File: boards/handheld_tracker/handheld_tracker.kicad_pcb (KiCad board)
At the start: 2 copper layers, 26 parts, among them SW1 SW_Push, SW10 SW_Push, SW11 SW_Push, SW12 SW_Push, SW13 SW_Push, SW14 SW_Push, SW15 SW_Push, SW2 SW_Push, SW3 SW_Push, SW4 SW_Push, SW5 SW_Push, SW6 SW_Push, SW7 SW_Push, SW8 SW_Push, SW9 SW_Push, U1 SAM-M8Q, U2 RFM96W-433S2, U3 ATmega328PB-A

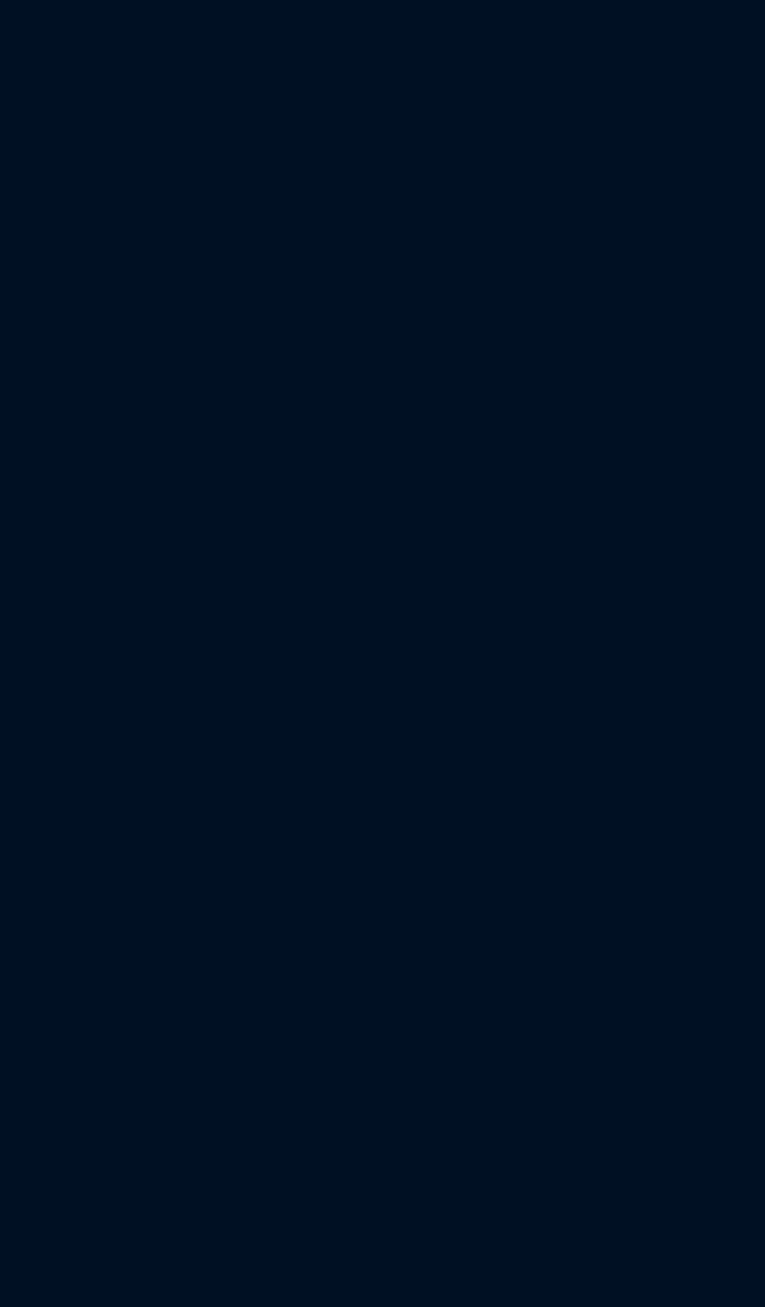
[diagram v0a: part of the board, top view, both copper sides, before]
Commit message: added all footprints and modified gitignore
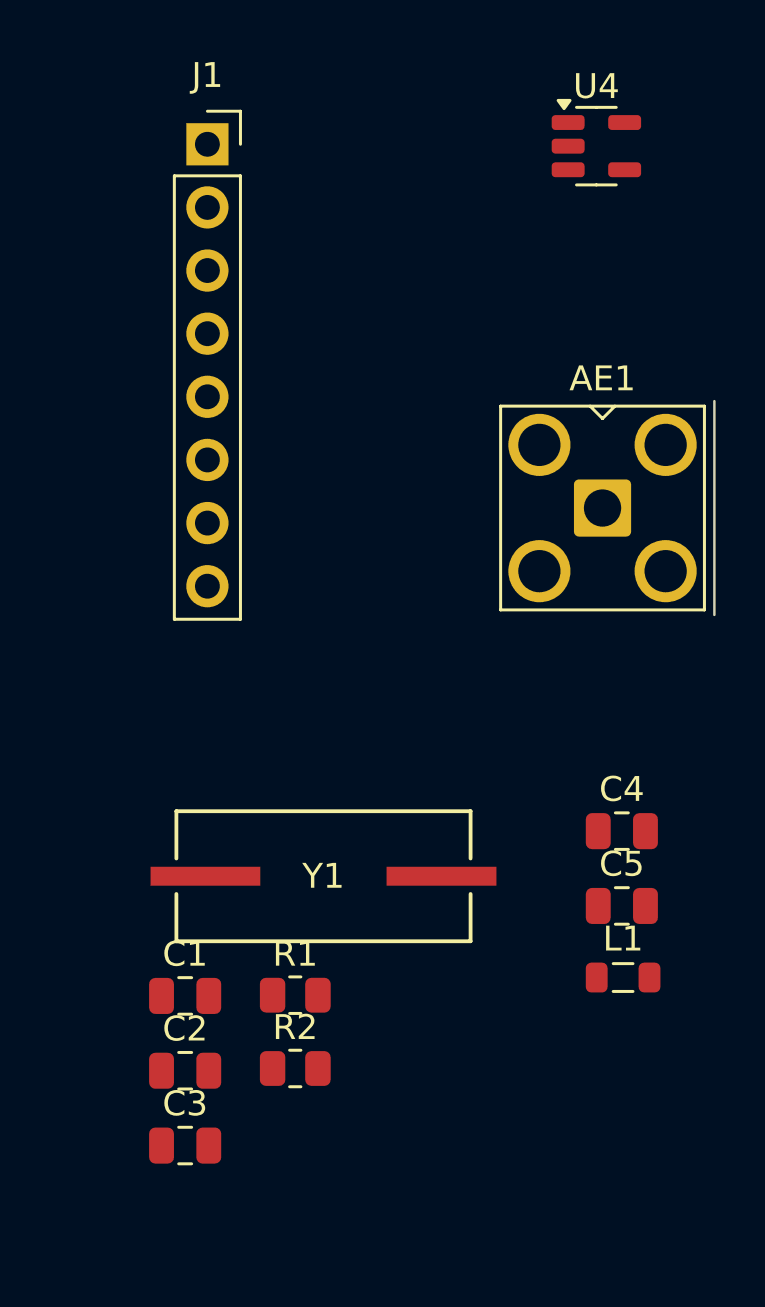
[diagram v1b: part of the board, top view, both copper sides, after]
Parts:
- added AE1: Antenna, Connector_Coaxial:SMA_Amphenol_901-143_Horizontal, F.Cu at (187.1, 83.1)
- added C1: 100nF, Capacitor_SMD:C_0805_2012Metric, F.Cu at (170.3, 102.7)
- added C2: 22pF, Capacitor_SMD:C_0805_2012Metric, F.Cu at (170.3, 105.8)
- added C3: 22pF, Capacitor_SMD:C_0805_2012Metric, F.Cu at (170.3, 108.8)
- added C4: 4.7uF, Capacitor_SMD:C_0805_2012Metric, F.Cu at (187.9, 96.1)
- added C5: 10 uF, Capacitor_SMD:C_0805_2012Metric, F.Cu at (187.9, 99.1)
- added J1: Conn_01x08_Pin, Connector_PinSocket_2.54mm:PinSocket_1x08_P2.54mm_Vertical, F.Cu at (171.2, 68.5)
- added L1: 2.2 uH, Inductor_SMD:L_0805_2012Metric, F.Cu at (187.9, 102.0)
- added R1: 1K, Resistor_SMD:R_0805_2012Metric, F.Cu at (174.7, 102.7)
- added R2: 1K, Resistor_SMD:R_0805_2012Metric, F.Cu at (174.7, 105.7)
- added U4: LM3670MF, Package_TO_SOT_SMD:TSOT-23-5, F.Cu at (186.9, 68.5)
- added Y1: Crystal, footprints:XTAL_ABLS-16_ABR, F.Cu at (175.9, 97.9)
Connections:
- U3 pad 22: /mcu/display_CS -> /display_RST

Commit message: basic pcb layout
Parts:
- added H1: MountingHole, MountingHole:MountingHole_2.5mm_Pad, F.Cu at (168.8, 40.5)
- added H2: MountingHole, MountingHole:MountingHole_2.5mm_Pad_TopBottom, F.Cu at (169.5, 50.5)
- added H3: MountingHole, MountingHole:MountingHole_2.5mm_Pad_TopBottom, F.Cu at (168.7, 67.6)
- added H4: MountingHole, MountingHole:MountingHole_2.5mm_Pad_TopBottom, F.Cu at (168.7, 74.2)
- moved AE1 90.2 mm to (112.5, 32.5), turned to 0 degrees
- moved TP_MISO1 74.1 mm to (200.0, 57.5)
- moved C4 73.9 mm to (259.7, 78.9)
- moved C5 73.9 mm to (259.7, 81.9)
- moved C1 73.9 mm to (242.2, 85.5)
- moved C2 73.9 mm to (242.2, 88.5)
- moved C3 73.9 mm to (242.2, 91.5)
- moved R1 73.9 mm to (246.6, 85.5)
- moved R2 73.9 mm to (246.6, 88.4)
- moved TP_3V3 73.9 mm to (209.8, 57.1)
- moved TP_GND1 73.9 mm to (214.8, 52.1)
- moved TP_I2C_SCL1 73.9 mm to (204.7, 57.1)
- moved TP_I2C_SDA1 73.9 mm to (209.8, 52.1)
- moved TP_INPUT_VOLTAGE1 73.9 mm to (214.8, 57.1)
- moved TP_MOSI1 73.9 mm to (204.7, 52.1)
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- renumbered SW11 to SW0, SW4 to SW2, SW7 to SW3, SW2 to SW4, SW8 to SW6, SW3 to SW7, SW6 to SW8, SW10 to SW_DOT1, SW15 to SW_DOWN1, SW12 to SW_ENTER1, SW13 to SW_MENU1, SW14 to SW_UP1, TP6 to TP_3V3, TP7 to TP_GND1, TP4 to TP_I2C_SCL1, TP5 to TP_I2C_SDA1, TP8 to TP_INPUT_VOLTAGE1, TP2 to TP_MISO1, TP3 to TP_MOSI1, TP1 to TP_SCK1
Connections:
- U1 pad 12: unconnected-(U1-SCL-Pad12) -> /I2C_SCL
- U1 pad 9: unconnected-(U1-SDA-Pad9) -> /I2C_SDA
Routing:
- net /pushbutton_enter: track 0.00 -> 40.5 mm, vias 0 -> 1
- net /pushbutton_dot: track 0.00 -> 40.5 mm, vias 0 -> 1
- net /pushbutton_0: track 0.00 -> 40.5 mm, vias 0 -> 1
- net /pushbutton_9: track 0.00 -> 29.0 mm, vias 0 -> 1
- net /pushbutton_8: track 0.00 -> 29.0 mm, vias 0 -> 1
- net /pushbutton_7: track 0.00 -> 29.0 mm, vias 0 -> 1
- net /pushbutton_6: track 0.00 -> 17.5 mm, vias 0 -> 1
- net /pushbutton_5: track 0.00 -> 17.5 mm, vias 0 -> 1
- net /pushbutton_4: track 0.00 -> 17.5 mm, vias 0 -> 1
- net /pushbutton_3: track 0.00 -> 6.00 mm, vias 0 -> 1
- net /pushbutton_2: track 0.00 -> 6.00 mm, vias 0 -> 1
- net /pushbutton_1: track 0.00 -> 6.00 mm, vias 0 -> 1
- added copper zone on B.Cu, net +3.3V
- added copper zone on B.Cu, net GND
- added copper zone on F.Cu, net GND

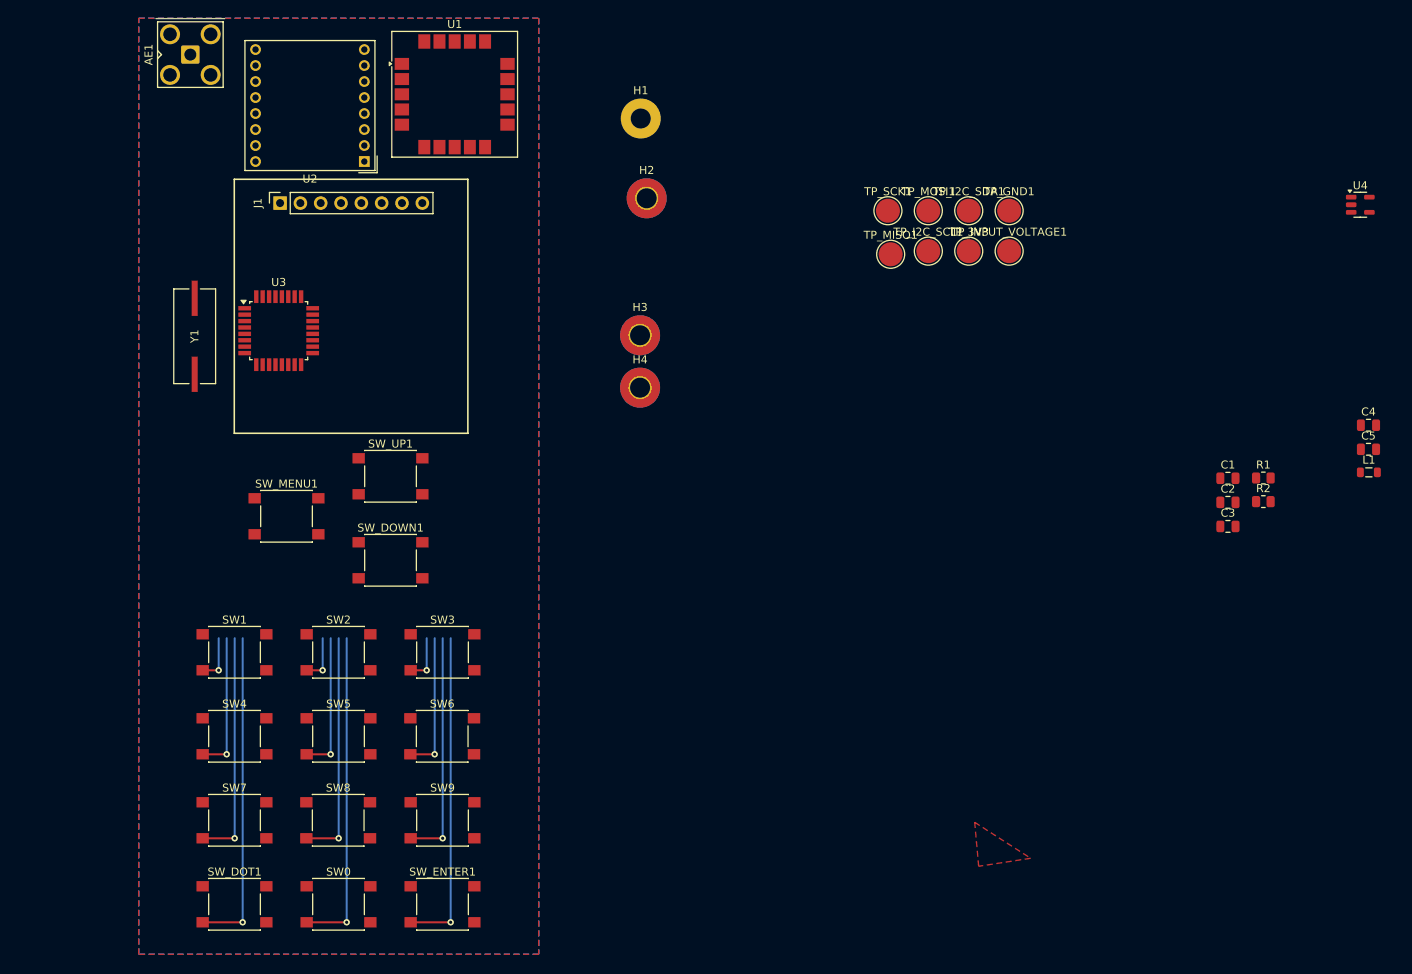
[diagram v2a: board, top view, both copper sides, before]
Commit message: added traces for buttons
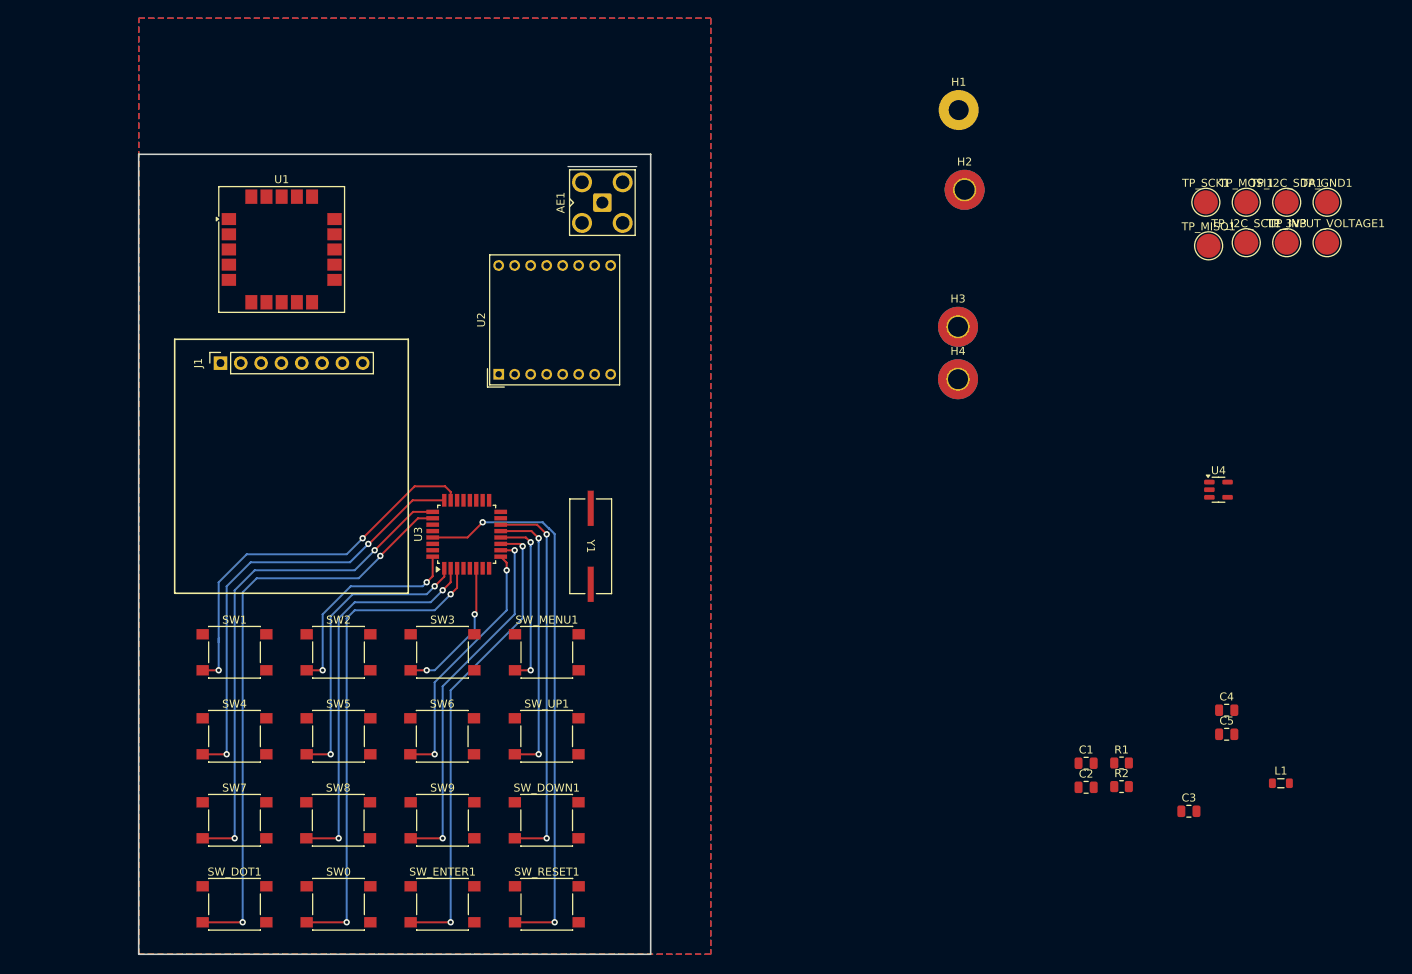
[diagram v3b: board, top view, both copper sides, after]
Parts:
- added SW_RESET1: SW_Push, Button_Switch_SMD:SW_SPST_PTS645, F.Cu at (157.0, 138.8)
- moved Y1 56.0 mm to (162.5, 94.0), turned to -90 degrees
- moved AE1 54.7 mm to (164.0, 51.0)
- moved L1 40.4 mm to (248.8, 123.6)
- moved C5 39.8 mm to (242.0, 117.5)
- moved C4 39.8 mm to (242.0, 114.5)
- moved U4 39.8 mm to (241.0, 86.9)
- moved C1 39.8 mm to (224.4, 121.1)
- moved C2 39.8 mm to (224.4, 124.1)
- moved R1 39.8 mm to (228.9, 121.1)
- moved R2 39.8 mm to (228.9, 124.0)
- moved H1 39.8 mm to (208.5, 39.5)
- moved H2 39.8 mm to (209.2, 49.4)
- moved H3 39.8 mm to (208.4, 66.6)
- moved H4 39.8 mm to (208.4, 73.1)
- moved TP_3V3 39.8 mm to (249.5, 56.0)
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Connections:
- TP_INPUT_VOLTAGE1 pad 1: /input_voltage -> INPUT_VOLTAGE
- U1 pad 3: unconnected-(U1-V_BCKP-Pad3) -> +3.3V
- U2 pad 5: /CS -> /transceiver_CS
- U3 pad 1: /pushbutton_8 -> /pushbutton_5
- U3 pad 10: /pushbutton_enter -> /pushbutton_9
- U3 pad 11: /pushbutton_menu -> /pushbutton_enter
- U3 pad 12: /pushbutton_1 -> /pushbutton_menu
- U3 pad 13: /pushbutton_2 -> /pushbutton_up
- U3 pad 14: /pushbutton_3 -> /pushbutton_down
- U3 pad 19: /mcu/transceiver_CS -> /transceiver_CS
- U3 pad 2: /pushbutton_dot -> /pushbutton_8
- U3 pad 23: /pushbutton_4 -> /pushbutton_1
- U3 pad 24: /pushbutton_5 -> /pushbutton_4
- U3 pad 25: /pushbutton_6 -> /pushbutton_7
- U3 pad 26: /pushbutton_7 -> /pushbutton_dot
- U3 pad 3: /pushbutton_up -> /pushbutton_0
- U3 pad 30: /mcu/TX -> /mcu/RX
- U3 pad 31: /mcu/RX -> /mcu/TX
- U3 pad 32: /pushbutton_9 -> /pushbutton_2
- U3 pad 6: /pushbutton_down -> /pushbutton_3
- U3 pad 9: /pushbutton_0 -> /pushbutton_6
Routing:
- net /mcu/RESET: track 0.00 -> 70.2 mm, vias 0 -> 2
- net /pushbutton_down: track 0.00 -> 48.2 mm, vias 0 -> 2
- net /pushbutton_1: track 6.00 -> 48.8 mm, vias 1 -> 2
- net /pushbutton_4: track 17.5 -> 55.7 mm, vias 1 -> 2
- net /pushbutton_up: track 0.00 -> 35.1 mm, vias 0 -> 2
- net /pushbutton_7: track 29.0 -> 63.8 mm, vias 1 -> 2
- net /pushbutton_dot: track 40.5 -> 73.9 mm, vias 1 -> 2
- net /pushbutton_menu: track 0.00 -> 22.0 mm, vias 0 -> 2
- net /pushbutton_2: track 6.00 -> 27.2 mm, vias 1 -> 2
- net /pushbutton_0: track 40.5 -> 60.8 mm, vias 1 -> 2
- net /pushbutton_8: track 29.0 -> 49.1 mm, vias 1 -> 2
- net /pushbutton_5: track 17.5 -> 37.6 mm, vias 1 -> 2
- net /pushbutton_enter: track 40.5 -> 58.6 mm, vias 1 -> 2
- net /pushbutton_9: track 29.0 -> 45.5 mm, vias 1 -> 2
- net /pushbutton_6: track 17.5 -> 31.7 mm, vias 1 -> 2
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- added copper zone on F.Cu, net +3.3V
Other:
- board outline added: 64 x 100 mm

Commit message: cleanup and trace work
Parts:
- added J2: Conn_01x02_Pin, Connector_PinHeader_2.54mm:PinHeader_1x02_P2.54mm_Vertical, F.Cu at (167.5, 79.2)
- moved TP_GND1 144.2 mm to (110.5, 56.5)
- moved TP_I2C_SDA1 138.5 mm to (111.0, 49.5)
- moved TP_I2C_SCL1 133.7 mm to (111.0, 63.5)
- moved C5 119.0 mm to (138.7, 58.5), turned to 90 degrees
- moved L1 118.7 mm to (144.2, 67.5), turned to 180 degrees
- moved TP_INPUT_VOLTAGE1 113.7 mm to (141.0, 49.5)
- moved C4 113.3 mm to (144.1, 57.5), turned to 180 degrees
- moved U4 100.0 mm to (144.0, 62.5), turned to -90 degrees
- moved TP_3V3 97.2 mm to (152.5, 49.5)
- moved TP_MOSI1 72.2 mm to (173.5, 64.5)
- moved TP_SCK1 69.0 mm to (173.5, 71.5)
- moved TP_MISO1 66.3 mm to (173.5, 57.5)
- moved C2 2.87 mm to (224.4, 127.0)
- moved U1 0.22 mm to (123.7, 56.9), turned to 180 degrees
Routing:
- net /mcu/TX: track 0.00 -> 31.4 mm, vias 0 -> 2
- net /mcu/RX: track 0.00 -> 29.8 mm, vias 0 -> 2
- net /I2C_SDA: track 0.00 -> 28.6 mm
- net /transceiver_CS: track 0.00 -> 27.9 mm
- net /MISO: track 0.00 -> 20.6 mm, vias 0 -> 2
- net /I2C_SCL: track 0.00 -> 18.9 mm
- net /MOSI: track 0.00 -> 18.8 mm
- net /SCK: track 0.00 -> 18.7 mm, vias 0 -> 2
- net +3.3V: track 0.00 -> 17.9 mm, vias 0 -> 3
- net Net-(U3-XTAL2/PB7): track 0.00 -> 16.6 mm
- net Net-(U3-XTAL1/PB6): track 0.00 -> 14.9 mm
- net GND: track 0.00 -> 9.04 mm
- net Net-(AE1-A): track 0.00 -> 8.29 mm
- net Net-(U4-SW): track 0.00 -> 3.98 mm
- net INPUT_VOLTAGE: track 0.00 -> 3.91 mm
- removed copper zone on F.Cu, net +3.3V
- removed copper zone on B.Cu, net GND

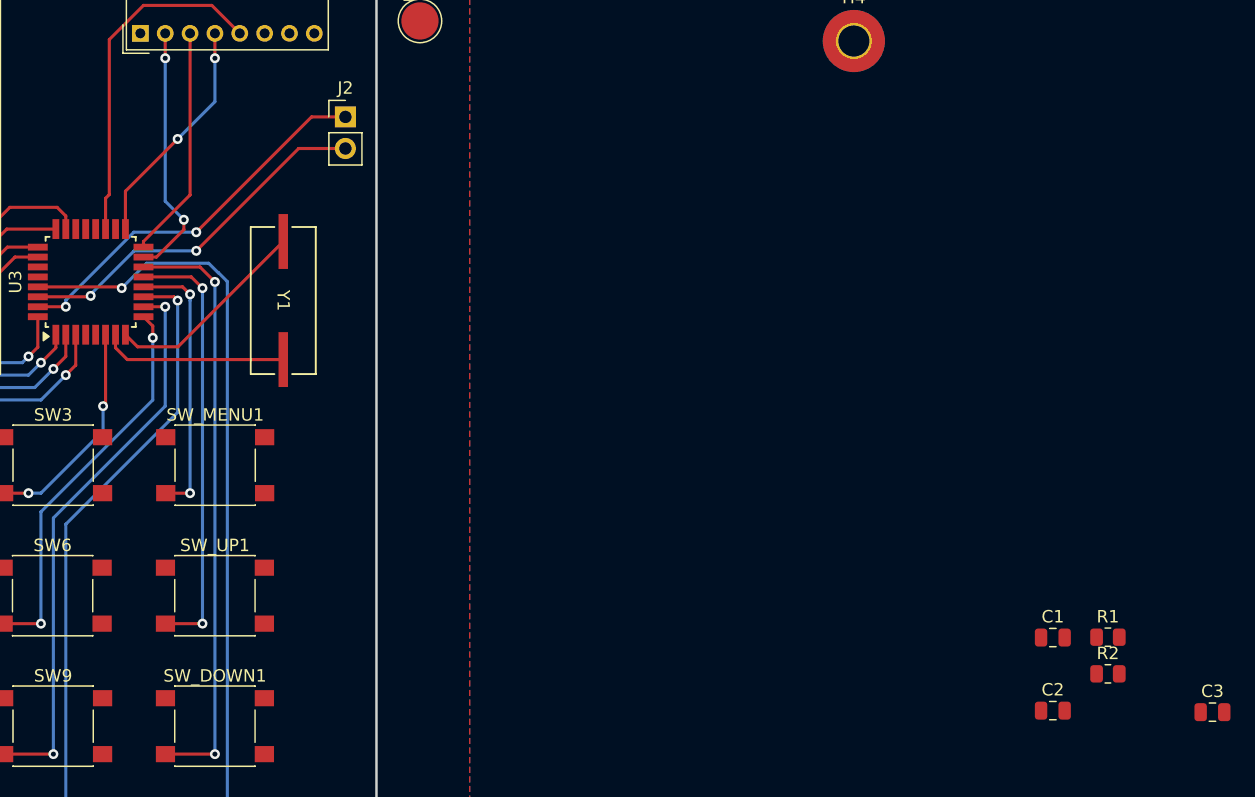
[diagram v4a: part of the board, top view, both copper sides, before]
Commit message: almost all stuff added and traced, just need proper 3.3 and GND planes plus the mounting holes I think
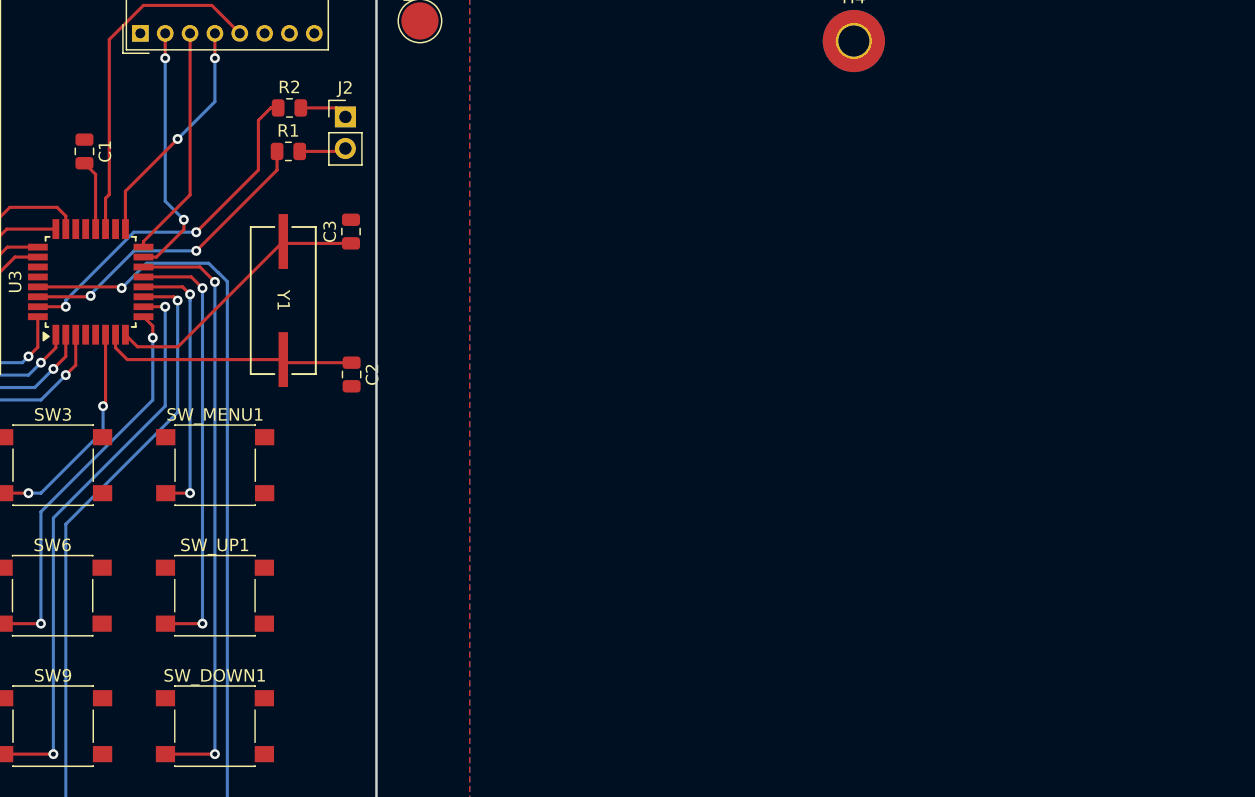
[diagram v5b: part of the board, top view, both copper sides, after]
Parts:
- R1, R2: value 1K -> 1k
- moved C1 87.2 mm to (146.5, 82.0), turned to -90 degrees
- moved R2 80.1 mm to (163.0, 78.5)
- moved C3 79.4 mm to (167.9, 88.5), turned to 90 degrees
- moved R1 76.7 mm to (162.9, 82.0)
- moved C2 62.6 mm to (168.0, 100.0), turned to -90 degrees
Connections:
- J2 pad 1: /mcu/TX -> Net-(J2-Pin_1)
- J2 pad 2: /mcu/RX -> Net-(J2-Pin_2)
- R1 pad 1: /mcu/TX -> /mcu/RX
- R1 pad 2: /mcu/TX -> Net-(J2-Pin_2)
- R2 pad 1: /mcu/RX -> /mcu/TX
- R2 pad 2: /mcu/RX -> Net-(J2-Pin_1)
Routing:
- net Net-(U3-AREF): track 0.00 -> 5.67 mm
- net Net-(U3-XTAL1/PB6): track 14.9 -> 20.5 mm
- net Net-(U3-XTAL2/PB7): track 16.6 -> 22.1 mm
- net /mcu/RX: track 29.8 -> 25.0 mm
- net Net-(J2-Pin_1): track 0.00 -> 3.89 mm
- net Net-(J2-Pin_2): track 0.00 -> 3.77 mm
- net /mcu/TX: track 31.4 -> 28.6 mm

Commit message: ignoring mounting holes for now
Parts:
- removed H1: MountingHole, MountingHole:MountingHole_2.5mm_Pad
- removed H2, H3, H4: MountingHole, MountingHole:MountingHole_2.5mm_Pad_TopBottom
- added R3: 10k, Resistor_SMD:R_0805_2012Metric, F.Cu at (165.1, 139.0)
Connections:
- SW_RESET1 pad 2: /mcu/RESET -> Net-(R3-Pad2)
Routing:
- net /mcu/RESET: track 70.3 -> 65.3 mm
- net Net-(R3-Pad2): track 0.00 -> 4.54 mm
